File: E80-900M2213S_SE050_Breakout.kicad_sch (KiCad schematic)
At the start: 18 parts, among them IC2 SE050E2HQ1_Z01Z3Z, J1 Conn_01x12_Pin, U1 E80-900M2213S

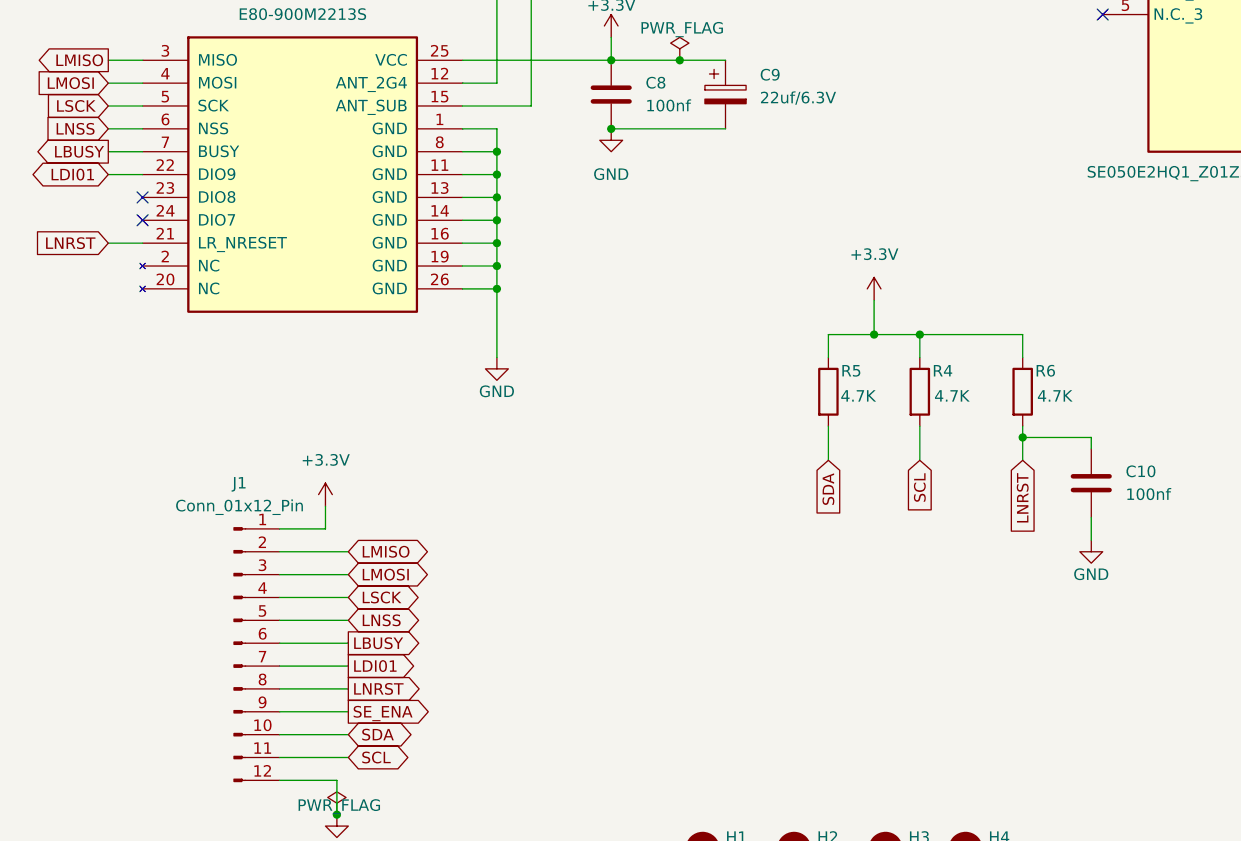
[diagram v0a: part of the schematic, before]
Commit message: Fix R6 to 10k and name the radio interrupt DIO9
R6, the pull-up on the module's NRESET line, was entered as 4.7k; the
intended value is 10k.

Header pin 7 carries the LR1121's interrupt, which the module brings out as
DIO9 on pin 22. The net and the silkscreen called it DIO1, the SX126x name,
so anyone wiring it by label would have looked for the wrong signal. The net
is now LDI09 and the legend reads DIO9. The copper is unchanged: the
regenerated copper gerbers draw the same geometry and differ only in the net
attribute.

Regenerate gerber/ and the zip, refresh both board images, and bring the
README's pinout and bill of materials in line.

Co-Authored-By: Claude Opus 5.5 <noreply@anthropic.com>
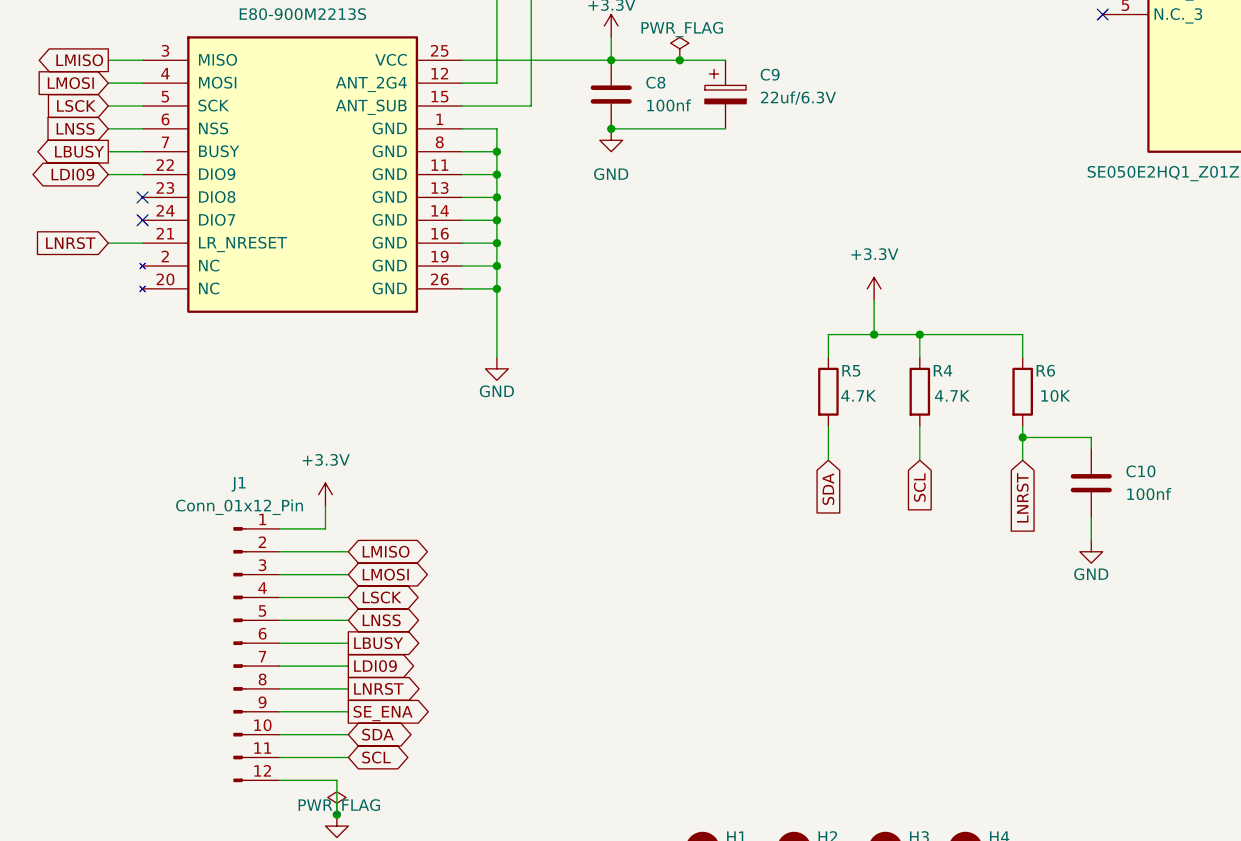
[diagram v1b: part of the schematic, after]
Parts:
- R6: value 4.7K -> 10K
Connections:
- net LDI01 renamed LDI09
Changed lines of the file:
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@@
 		)
 	)
-	(global_label "LDI01"
+	(global_label "LDI09"
 		(shape bidirectional)
 		(at 60.96 106.68 180)
@@
 		)
 	)
-	(global_label "LDI01"
+	(global_label "LDI09"
 		(shape output)
 		(at 87.63 161.29 0)
@@
 			)
 		)
-		(property "Value" "4.7K"
+		(property "Value" "10K"
 			(at 166.116 131.318 0)
 			(show_name no)

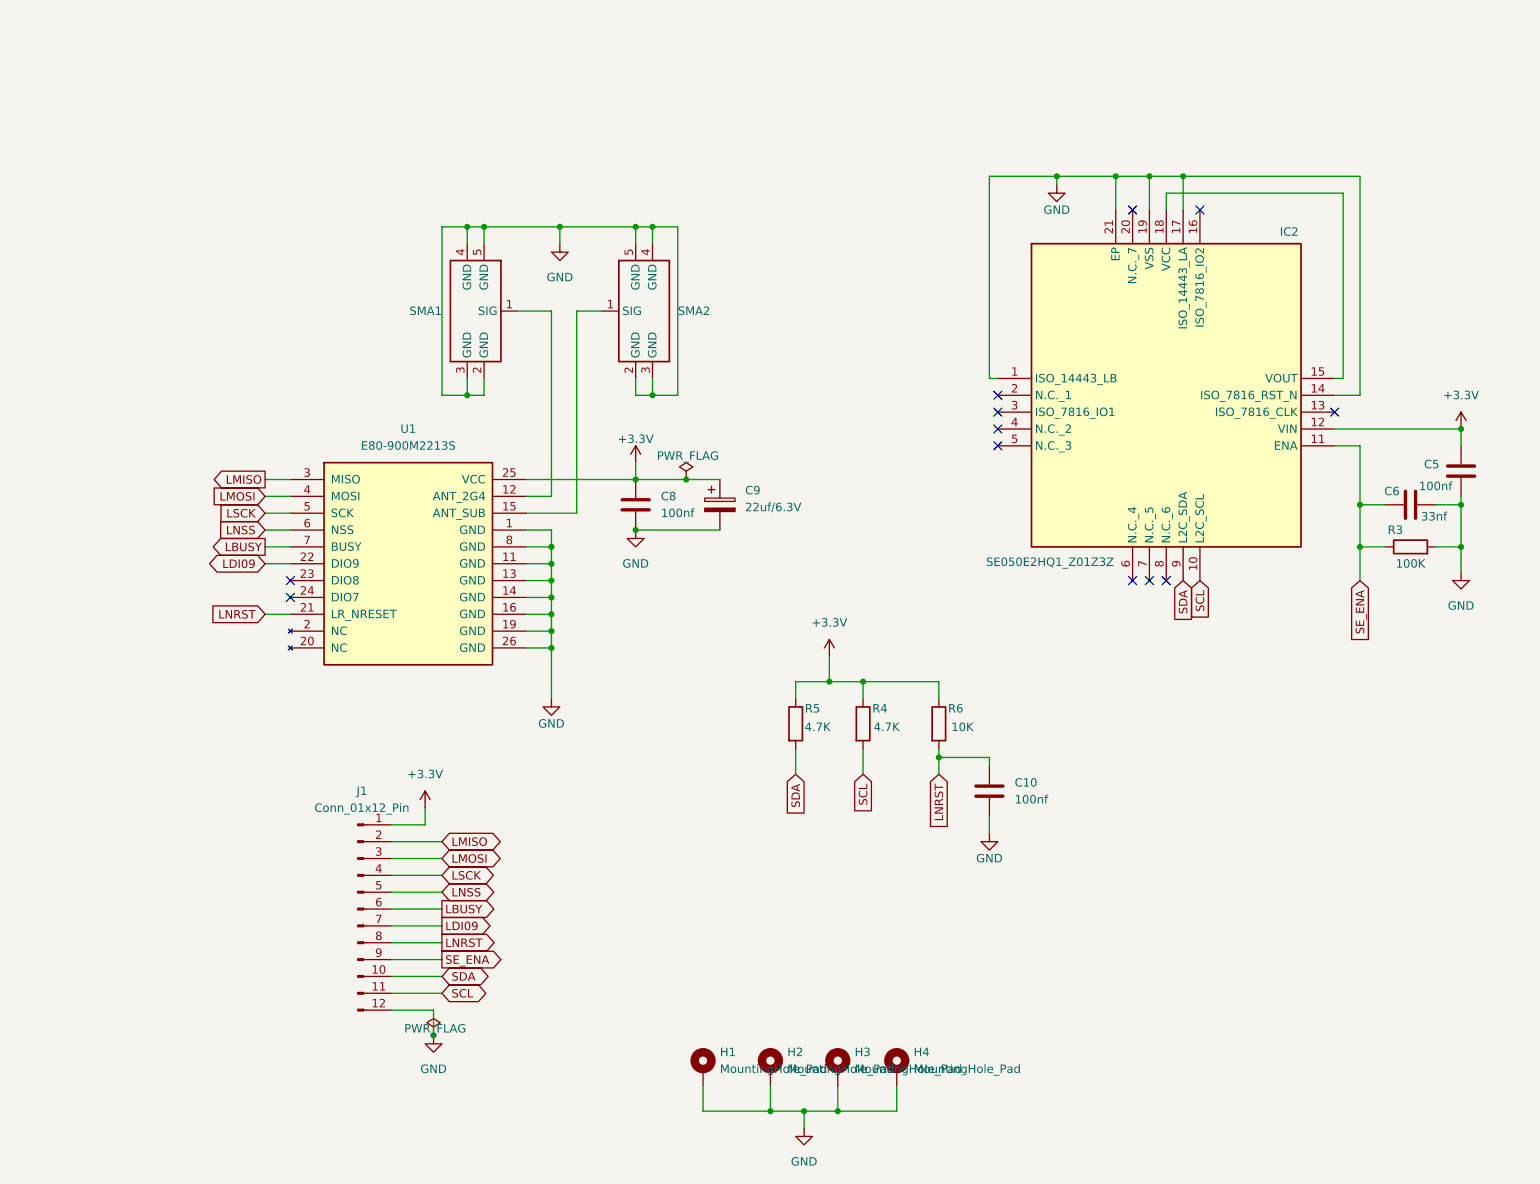
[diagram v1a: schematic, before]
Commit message: Widen the host header to 14 pins and ground the SE050 pad through five vias
The host connector is now a 1x14 2.54 mm header (J2) instead of the
1x12 2.00 mm one. The two extra pins bring out the LR1121's DIO7 and DIO8
(module pins 24 and 23), which were left unconnected before. The other
signals keep their order and move down two positions: DIO9 is now pin 9,
NRST 10, ENA 11, SDA 12, SCL 13 and GND 14.

The SE050's exposed pad had a single via to the ground plane, in its
centre. Four more 0.3 mm vias go under the four paste windows, which is
the five-via pattern of the se050-breakout board that was validated on
hardware.

Regenerate gerber/ and the zip (297 plated holes: 237 vias and 60 pads),
refresh both board images, and update the README's pinout, bill of
materials and hole count.

Co-Authored-By: Claude Opus 5.5 <noreply@anthropic.com>
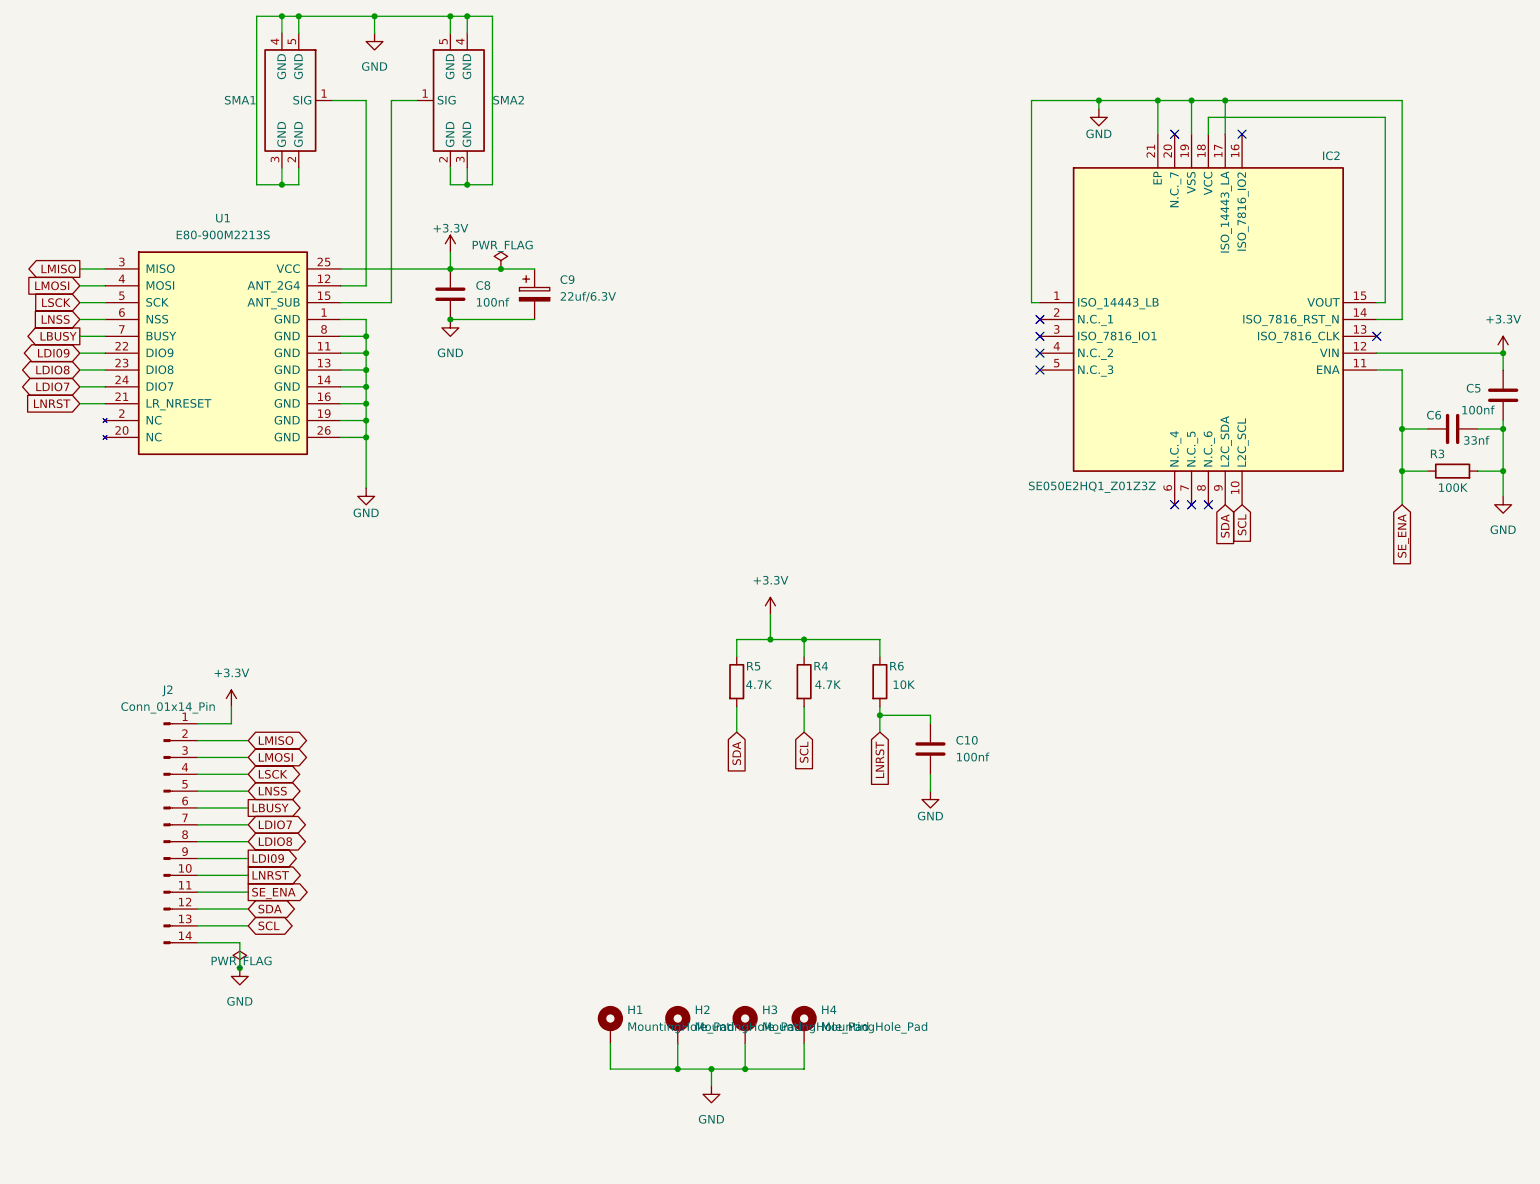
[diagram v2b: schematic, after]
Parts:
- removed J1: Conn_01x12_Pin, Connector_PinHeader_2.00mm:PinHeader_1x12_P2.00mm_Vertical, symbol Connector:Conn_01x12_Pin
- added J2: Conn_01x14_Pin, Connector_PinHeader_2.54mm:PinHeader_1x14_P2.54mm_Vertical, symbol Connector:Conn_01x14_Pin
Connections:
- net +3.3V: now also J2.1 (Pin_1)
- net GND: now also J2.14 (Pin_14)
- net LBUSY: now also J2.6 (Pin_6)
- net LDI09: now also J2.9 (Pin_9)
- net LMISO: now also J2.2 (Pin_2)
- net LMOSI: now also J2.3 (Pin_3)
- net LNRST: now also J2.10 (Pin_10)
- net LNSS: now also J2.5 (Pin_5)
- net LSCK: now also J2.4 (Pin_4)
- net SCL: now also J2.13 (Pin_13)
- net SDA: now also J2.12 (Pin_12)
- net SE_ENA: now also J2.11 (Pin_11)
- net LDIO8: now reaches U1.23 (DIO8)
- net LDIO8: now also J2.8 (Pin_8)
- net LDIO7: now reaches U1.24 (DIO7)
- net LDIO7: now also J2.7 (Pin_7)
- no-connect marks 12 -> 10
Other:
- moved on the sheet: C10, C5, C6, C8, C9, H1, H2, H3, H4, IC2, R3, R4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
